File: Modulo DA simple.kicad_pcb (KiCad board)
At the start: 2 copper layers, 105.9 x 41.5 mm, 49 parts, among them J1 PJ-625C, J2 PJ-625C, J3 Conn_01x04, J4 PJ-625C, J5 PJ-625C, J6 Conn_02x04_Counter_Clockwise, J7 Conn_01x04, J8 Conn_01x04, U1 PCM5100APWR, U2 WM8782SEDS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

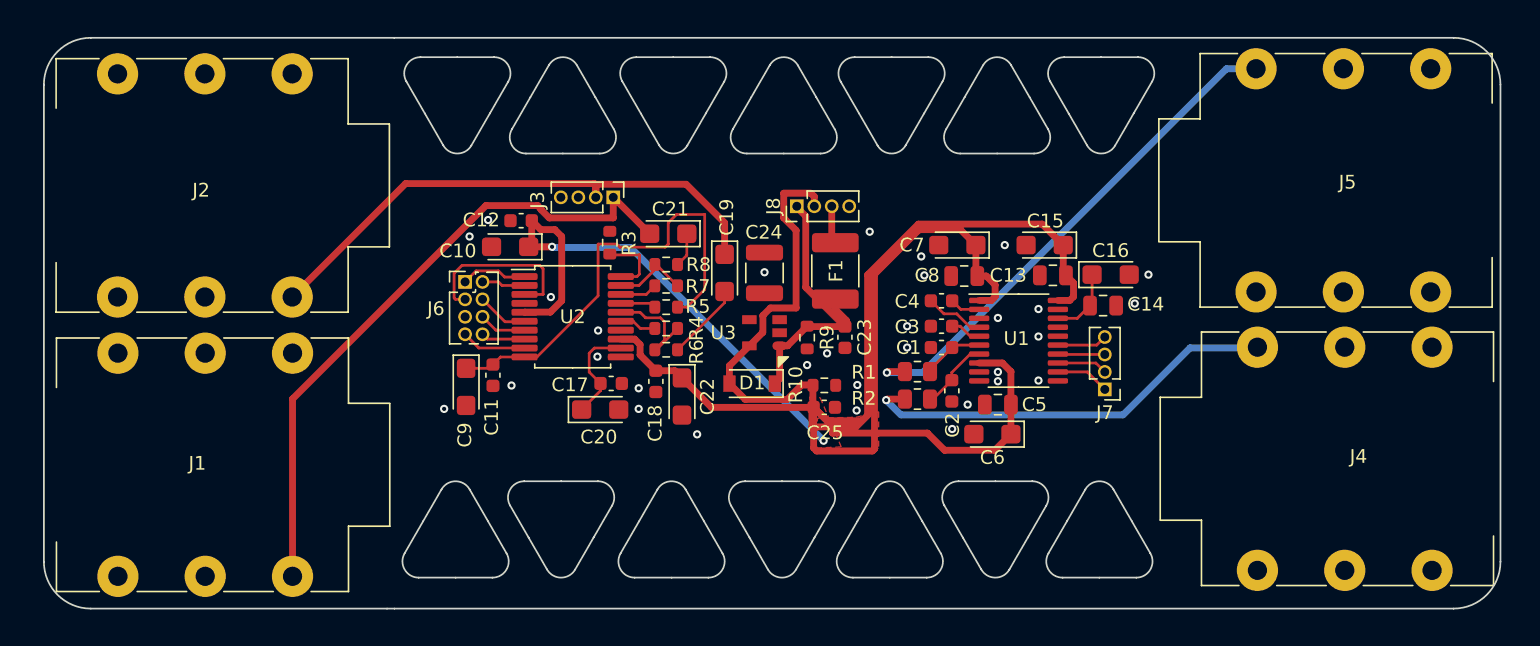
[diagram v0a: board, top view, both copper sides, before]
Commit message: add gnd and gnda in the pcb
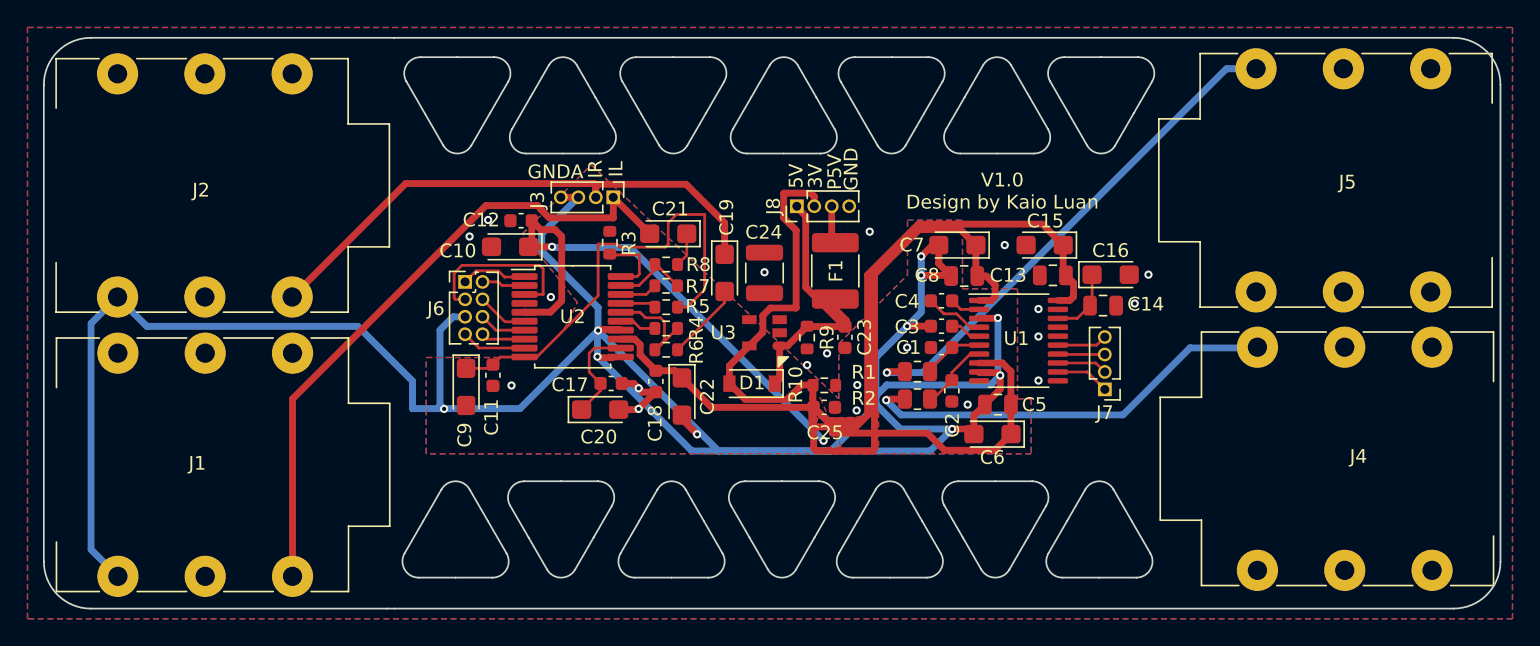
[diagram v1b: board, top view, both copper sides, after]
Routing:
- net GNDA: track 0.00 -> 203.7 mm
- net GND: vias 18 -> 17
- added copper zone on B.Cu, net GND
- added copper zone on F.Cu, net GND
- added copper zone on B.Cu, net GNDA
- added copper zone on F.Cu, net GNDA
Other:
- board text added: "3V"
- board text added: "5V"
- board text added: "GND"
- board text added: "GNDA"
- board text added: "IL"
- board text added: "IR"
- board text added: "P5V"
- board text added: "V1.0 Design by Kaio Luan"

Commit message: 01092022
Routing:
- net GND: vias 17 -> 23
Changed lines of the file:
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@@
   (via (at 167.525 106.475) (size 0.6) (drill 0.3) (layers "F.Cu" "B.Cu") (free) (net 2))
   (via (at 154.3 111.85) (size 0.6) (drill 0.3) (layers "F.Cu" "B.Cu") (free) (net 2))
+  (via (at 125.8 96.7) (size 0.6) (drill 0.3) (layers "F.Cu" "B.Cu") (free) (net 2))
+  (via (at 134.8 102) (size 0.6) (drill 0.3) (layers "F.Cu" "B.Cu") (free) (net 2))
+  (via (at 124.1 98.3) (size 0.6) (drill 0.3) (layers "F.Cu" "B.Cu") (free) (net 2))
   (via (at 162.375 111.425) (size 0.6) (drill 0.3) (layers "F.Cu" "B.Cu") (free) (net 2))
   (via (at 157.975 107.275) (size 0.6) (drill 0.3) (layers "F.Cu" "B.Cu") (free) (net 2))
   (via (at 152.15 107.7) (size 0.6) (drill 0.3) (layers "F.Cu" "B.Cu") (free) (net 2))
+  (via (at 138.8 96.6) (size 0.6) (drill 0.3) (layers "F.Cu" "B.Cu") (free) (net 2))
   (via (at 174.525 104.075) (size 0.6) (drill 0.3) (layers "F.Cu" "B.Cu") (free) (net 2))
   (via (at 147.6 101.8) (size 0.6) (drill 0.3) (layers "F.Cu" "B.Cu") (free) (net 2))
@@
   (via (at 154.35 110) (size 0.6) (drill 0.3) (layers "F.Cu" "B.Cu") (free) (net 2))
   (via (at 150.7 108.55) (size 0.6) (drill 0.3) (layers "F.Cu" "B.Cu") (free) (net 2))
+  (via (at 133.7 104.3) (size 0.6) (drill 0.3) (layers "F.Cu" "B.Cu") (free) (net 2))
+  (via (at 120.2 101.7) (size 0.6) (drill 0.3) (layers "F.Cu" "B.Cu") (free) (net 2))
   (via (at 167.525 109.675) (size 0.6) (drill 0.3) (layers "F.Cu" "B.Cu") (free) (net 2))
   (segment (start 161.225 109.084315) (end 162.559315 107.75) (width 0.2) (layer "F.Cu") (net 3))
@@
   (segment (start 141.6 109.487715) (end 143.737285 111.625) (width 0.5) (layer "F.Cu") (net 8))
   (segment (start 138.55 107.055608) (end 138.157107 106.662715) (width 0.5) (layer "F.Cu") (net 8))
-  (segment (start 154.25 113.05) (end 151.05 113.05) (width 0.5) (layer "F.Cu") (net 8))
   (segment (start 164.375 102.725) (end 163.725 102.075) (width 0.5) (layer "F.Cu") (net 8))
   (segment (start 132.15 99.95) (end 130.45 99.95) (width 0.5) (layer "F.Cu") (net 8))
   (segment (start 152.55 113) (end 151.175 111.625) (width 0.5) (layer "F.Cu") (net 8))
   (segment (start 155.453554 114.8) (end 151.396446 114.8) (width 0.5) (layer "F.Cu") (net 8))
-  (segment (start 151.05 113.05) (end 151.05 111.85) (width 0.5) (layer "F.Cu") (net 8))
   (segment (start 165.525 113.575) (end 165.525 111.425) (width 0.5) (layer "F.Cu") (net 8))
   (segment (start 151.125 111.575) (end 151.175 111.625) (width 0.5) (layer "F.Cu") (net 8))
@@
   (segment (start 158.789339 98.3) (end 155.1 101.989339) (width 0.5) (layer "F.Cu") (net 8))
   (segment (start 164.1 103.85) (end 164.375 103.575) (width 0.5) (layer "F.Cu") (net 8))
+  (segment (start 151.55 112) (end 151.55 113.05) (width 0.5) (layer "F.Cu") (net 8))
   (segment (start 170.075 103.575) (end 170.075 102.575) (width 0.5) (layer "F.Cu") (net 8))
-  (segment (start 151.05 111.75) (end 151.175 111.625) (width 0.5) (layer "F.Cu") (net 8))
   (segment (start 130.162715 104.7) (end 130.15 104.712715) (width 0.5) (layer "F.Cu") (net 8))
+  (segment (start 154.25 113.05) (end 151.55 113.05) (width 0.5) (layer "F.Cu") (net 8))
   (segment (start 130.675 98.05) (end 131.325 98.7) (width 0.5) (layer "F.Cu") (net 8))
   (segment (start 139.7 108.962715) (end 138.55 107.812715) (width 0.5) (layer "F.Cu") (net 8))
@@
   (segment (start 151.125 110.025) (end 151.125 111.575) (width 0.5) (layer "F.Cu") (net 8))
   (segment (start 155.1 101.989339) (end 155.1 112.2) (width 0.5) (layer "F.Cu") (net 8))
+  (segment (start 151.175 111.625) (end 151.55 112) (width 0.5) (layer "F.Cu") (net 8))
   (segment (start 149.9 98.75) (end 149.9 104.4) (width 0.5) (layer "F.Cu") (net 8))
-  (segment (start 151.05 111.85) (end 151.05 111.75) (width 0.5) (layer "F.Cu") (net 8))
   (segment (start 155.6 114.653554) (end 155.453554 114.8) (width 0.5) (layer "F.Cu") (net 8))
   (segment (start 159.45 113.5) (end 152.55 113.5) (width 0.5) (layer "F.Cu") (net 8))
@@
         (xy 123 108)
         (xy 131 108)
-        (xy 133 106)
-        (xy 134 104)
+        (xy 131.5 106.7)
+        (xy 131.5 101.2)
         (xy 130 99)
         (xy 135 94)
@@
     (polygon
       (pts
-        (xy 153.178568 114.5)
-        (xy 151.1 114.6)
-        (xy 150.885423 110.864185)
-        (xy 151.649377 110.92071)
+        (xy 153.5 114.5)
+        (xy 150.6 114.618161)
+        (xy 150.569235 110.882346)
+        (xy 153.5 110.9)
       )
     )

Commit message: 02092022
Check and connection some components
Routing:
- net GNDA: track 203.7 -> 271.0 mm, vias 13 -> 15
- net GND: track 0.15 -> 3.44 mm, vias 23 -> 36
- net Net-(C24-Pad1): track 0.00 -> 2.38 mm
- net 5V: track 20.8 -> 22.8 mm
- net AINL_JACK: track 47.7 -> 49.1 mm
- net OUTR_JACK: track 30.9 -> 30.4 mm
- removed copper zone on B.Cu, net GNDA
- removed copper zone on F.Cu, net GNDA

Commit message: 02092022-1
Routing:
- net GND: track 3.44 -> 7.50 mm
- net GNDA: track 271.0 -> 273.0 mm
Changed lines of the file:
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@@
   (segment (start 159.6375 108.8875) (end 161.25 107.275) (width 0.2) (layer "F.Cu") (net 1))
   (segment (start 174.125 101.975) (end 174.125 101.825) (width 0.5) (layer "F.Cu") (net 2))
+  (segment (start 162.375 110.5375) (end 162.3 110.4625) (width 0.5) (layer "F.Cu") (net 2))
+  (segment (start 167.55 106.45) (end 168.9375 106.45) (width 0.5) (layer "F.Cu") (net 2))
   (segment (start 147.6 106.8) (end 147.694949 106.8) (width 0.5) (layer "F.Cu") (net 2))
+  (segment (start 162.3 110.4625) (end 162.3 109.7) (width 0.5) (layer "F.Cu") (net 2))
+  (segment (start 167.525 106.475) (end 167.55 106.45) (width 0.5) (layer "F.Cu") (net 2))
   (segment (start 130.15 104.062715) (end 131.676278 104.062715) (width 0.5) (layer "F.Cu") (net 2))
+  (segment (start 162.375 111.1) (end 162.375 110.5375) (width 0.5) (layer "F.Cu") (net 2))
   (segment (start 148.294949 106.2) (end 148.7 106.2) (width 0.5) (layer "F.Cu") (net 2))
+  (segment (start 167.55 104.5) (end 168.2 104.5) (width 0.5) (layer "F.Cu") (net 2))
   (segment (start 131.676278 104.062715) (end 131.969497 103.769496) (width 0.5) (layer "F.Cu") (net 2))
+  (segment (start 162.3 109.7) (end 162.822551 109.7) (width 0.5) (layer "F.Cu") (net 2))
   (segment (start 147.694949 106.8) (end 148.294949 106.2) (width 0.5) (layer "F.Cu") (net 2))
+  (segment (start 167.525 104.475) (end 167.55 104.5) (width 0.5) (layer "F.Cu") (net 2))
   (via (at 175.525 101.975) (size 0.6) (drill 0.3) (layers "F.Cu" "B.Cu") (free) (net 2))
   (via (at 186.4 112.5) (size 0.6) (drill 0.3) (layers "F.Cu" "B.Cu") (free) (net 2))
@@
   (via (at 134.8 102) (size 0.6) (drill 0.3) (layers "F.Cu" "B.Cu") (free) (net 2))
   (via (at 124.1 98.3) (size 0.6) (drill 0.3) (layers "F.Cu" "B.Cu") (free) (net 2))
-  (via (at 162.375 111.425) (size 0.6) (drill 0.3) (layers "F.Cu" "B.Cu") (free) (net 2))
+  (via (at 162.375 111.1) (size 0.6) (drill 0.3) (layers "F.Cu" "B.Cu") (free) (net 2))
   (via (at 157.975 107.275) (size 0.6) (drill 0.3) (layers "F.Cu" "B.Cu") (free) (net 2))
   (via (at 132.1 105.8) (size 0.6) (drill 0.3) (layers "F.Cu" "B.Cu") (free) (net 2))
@@
   (segment (start 162.45 113.2) (end 162.825 113.575) (width 0.5) (layer "F.Cu") (net 5))
   (segment (start 164.745023 109.304977) (end 164.540046 109.1) (width 0.5) (layer "F.Cu") (net 5))
+  (segment (start 125.9 111.487715) (end 124.25 111.487715) (width 0.5) (layer "F.Cu") (net 5))
   (segment (start 135.525 108.012715) (end 136.563173 108.012715) (width 0.5) (layer "F.Cu") (net 5))
   (segment (start 129.175 110.062715) (end 129.2 110.037715) (width 0.5) (layer "F.Cu") (net 5))
@@
   (segment (start 160.275 101.175) (end 161.175 102.075) (width 0.5) (layer "F.Cu") (net 5))
   (segment (start 161.25 113.2) (end 162.45 113.2) (width 0.5) (layer "F.Cu") (net 5))
+  (segment (start 124.25 111.487715) (end 124 111.737715) (width 0.5) (layer "F.Cu") (net 5))
   (segment (start 132.79 96.35) (end 134.06 96.35) (width 0.5) (layer "F.Cu") (net 5))
   (segment (start 164 109.1) (end 163.2125 109.1) (width 0.5) (layer "F.Cu") (net 5))
